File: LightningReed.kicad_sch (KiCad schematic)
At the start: 163 parts, among them P1 Conn_WallPlug, Q1 NCE65T180D, Q10 DMZ6005E, Q11 2N7002K, Q12 NCEP15T14D, Q13 BSS123, Q2 2N7002, Q3 Q_NMOS_GDS, Q4 2N7002, Q5 2N7002K, Q6 2N7002K, Q7 NCE65T260K, Q8 NCE65T260K, Q9 NCE0102, T1 Transformer_2P_2S, U1 UCC28056, U2 78L05S, U3 LMC7111, U4 UCC28780, U5 UCC27712, U6 LM317G, U7 FODM8801A, U8 TL431DBZ, U9 UCC24612-1DBV

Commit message: C Footprint
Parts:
- C11, C12, C13, C14, C15, C23, C24, C25, C26, C30, C31, C32, C33, C34, C35, C36, C37, C38, C44, C45, C46, C47: footprint (none) -> Capacitor_SMD:C_0603_1608Metric
- C16, C28: footprint (none) -> Capacitor_SMD:C_0805_2012Metric
- C17: value 33nF -> 220pF; footprint (none) -> Capacitor_SMD:C_0603_1608Metric
- C18, C39, C40, C41, C42: footprint (none) -> Capacitor_SMD:C_1206_3216Metric
- C19: footprint (none) -> Capacitor_SMD:C_1812_4532Metric
- C20, C21, C22, C27, C29: footprint (none) -> Capacitor_SMD:C_1210_3225Metric
- C43: footprint (none) -> Capacitor_SMD:CP_Elec_10x10
- D1: footprint (none) -> Diode_SMD:D_SMF
- D2: footprint (none) -> LightningReed:UMSB
- D3, D5: footprint (none) -> Diode_SMD:D_SOD-123F
- D4: footprint (none) -> Diode_SMD:D_SOD-323
- D6: footprint (none) -> Diode_SMD:D_SOD-123
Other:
- note added: "VZT681M1ETR-1010"
- moved on the sheet: R49

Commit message: Footprints
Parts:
- D10, D15: footprint (none) -> Diode_SMD:D_SOD-123
- D11, D13, D14, D16: footprint (none) -> Diode_SMD:D_SOD-323
- D12: footprint (none) -> Package_TO_SOT_SMD:SOT-23
- D17: footprint (none) -> Diode_SMD:D_SOD-523
- D7: value ES1JAF -> STTH1R06A; footprint (none) -> Diode_SMD:D_SMA
- D8, D9: footprint (none) -> Diode_SMD:D_SOD-123F
- L1, L2: footprint (none) -> LightningReed:CHOKE
- L3: value PDMTAT068125-151MLU -> SDA0912-150uH-0.45; footprint (none) -> Inductor_THT:L_Radial_D12.0mm_P5.00mm_Fastron_11P
- L4: footprint (none) -> Inductor_SMD:L_12x12mm_H8mm
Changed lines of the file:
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@@
       (effects (font (size 0.8 0.8)))
     )
-    (property "Footprint" "" (at 266.065 78.74 90)
+    (property "Footprint" "Diode_SMD:D_SOD-123" (at 266.065 78.74 90)
       (effects (font (size 1.27 1.27)) hide)
     )
@@
       (effects (font (size 1.27 1.27)))
     )
-    (property "Footprint" "" (at 57.785 31.75 0)
+    (property "Footprint" "LightningReed:CHOKE" (at 57.785 31.75 0)
       (effects (font (size 1.27 1.27)) hide)
     )
@@
       (effects (font (size 0.8 0.8)) (justify left))
     )
-    (property "Footprint" "" (at 252.73 130.81 90)
+    (property "Footprint" "Diode_SMD:D_SOD-323" (at 252.73 130.81 90)
       (effects (font (size 1.27 1.27)) hide)
     )
@@
       (effects (font (size 1.27 1.27)) (justify right))
     )
-    (property "Footprint" "" (at 293.37 79.375 90)
+    (property "Footprint" "Diode_SMD:D_SOD-523" (at 293.37 79.375 90)
       (effects (font (size 1.27 1.27)) hide)
     )
@@
       (effects (font (size 0.8 0.8)) (justify left))
     )
-    (property "Footprint" "" (at 271.145 97.79 90)
+    (property "Footprint" "Diode_SMD:D_SOD-323" (at 271.145 97.79 90)
       (effects (font (size 1.27 1.27)) hide)
     )
@@
       (effects (font (size 0.8 0.8)))
     )
-    (property "Footprint" "" (at 226.06 95.25 90)
+    (property "Footprint" "Package_TO_SOT_SMD:SOT-23" (at 226.06 95.25 90)
       (effects (font (size 1.27 1.27)) hide)
     )
@@
       (effects (font (size 0.8 0.8)) (justify left))
     )
-    (property "Footprint" "" (at 241.3 130.81 90)
+    (property "Footprint" "Diode_SMD:D_SOD-323" (at 241.3 130.81 90)
       (effects (font (size 1.27 1.27)) hide)
     )
@@
       (effects (font (size 1.27 1.27)))
     )
-    (property "Footprint" "" (at 84.455 31.75 0)
+    (property "Footprint" "LightningReed:CHOKE" (at 84.455 31.75 0)
       (effects (font (size 1.27 1.27)) hide)
     )
@@
       (effects (font (size 1.27 1.27)))
     )
-    (property "Value" "PDMTAT068125-151MLU" (at 38.735 53.34 90)
+    (property "Value" "SDA0912-150uH-0.45" (at 38.735 53.34 90)
       (effects (font (size 1.27 1.27)))
     )
-    (property "Footprint" "" (at 38.735 56.515 0)
+    (property "Footprint" "Inductor_THT:L_Radial_D12.0mm_P5.00mm_Fastron_11P" (at 38.735 56.515 0)
       (effects (font (size 1.27 1.27)) hide)
     )
@@
       (effects (font (size 1.27 1.27)))
     )
-    (property "Value" "ES1JAF" (at 187.325 40.64 0)
+    (property "Value" "STTH1R06A" (at 189.865 41.91 0)
       (effects (font (size 1.27 1.27)))
     )
-    (property "Footprint" "" (at 191.77 39.37 90)
+    (property "Footprint" "Diode_SMD:D_SMA" (at 191.77 39.37 90)
       (effects (font (size 1.27 1.27)) hide)
     )
@@
       (effects (font (size 0.8 0.8)) (justify right))
     )
-    (property "Footprint" "" (at 235.585 69.215 90)
+    (property "Footprint" "Diode_SMD:D_SOD-123F" (at 235.585 69.215 90)
       (effects (font (size 1.27 1.27)) hide)
     )
@@
       (effects (font (size 0.8 0.8)) (justify right))
     )
-    (property "Footprint" "" (at 207.01 90.805 90)
+    (property "Footprint" "Diode_SMD:D_SOD-323" (at 207.01 90.805 90)
       (effects (font (size 1.27 1.27)) hide)
     )
@@
       (effects (font (size 1.27 1.27)))
     )
-    (property "Footprint" "" (at 63.5 62.865 0)
+    (property "Footprint" "Inductor_SMD:L_12x12mm_H8mm" (at 63.5 62.865 0)
       (effects (font (size 1.27 1.27)) hide)
     )
@@
       (effects (font (size 0.8 0.8)) (justify right))
     )
-    (property "Footprint" "" (at 240.665 69.215 90)
+    (property "Footprint" "Diode_SMD:D_SOD-123F" (at 240.665 69.215 90)
       (effects (font (size 1.27 1.27)) hide)
     )
@@
       (effects (font (size 0.8 0.8)) (justify right))
     )
-    (property "Footprint" "" (at 220.345 81.28 90)
+    (property "Footprint" "Diode_SMD:D_SOD-123" (at 220.345 81.28 90)
       (effects (font (size 1.27 1.27)) hide)
     )

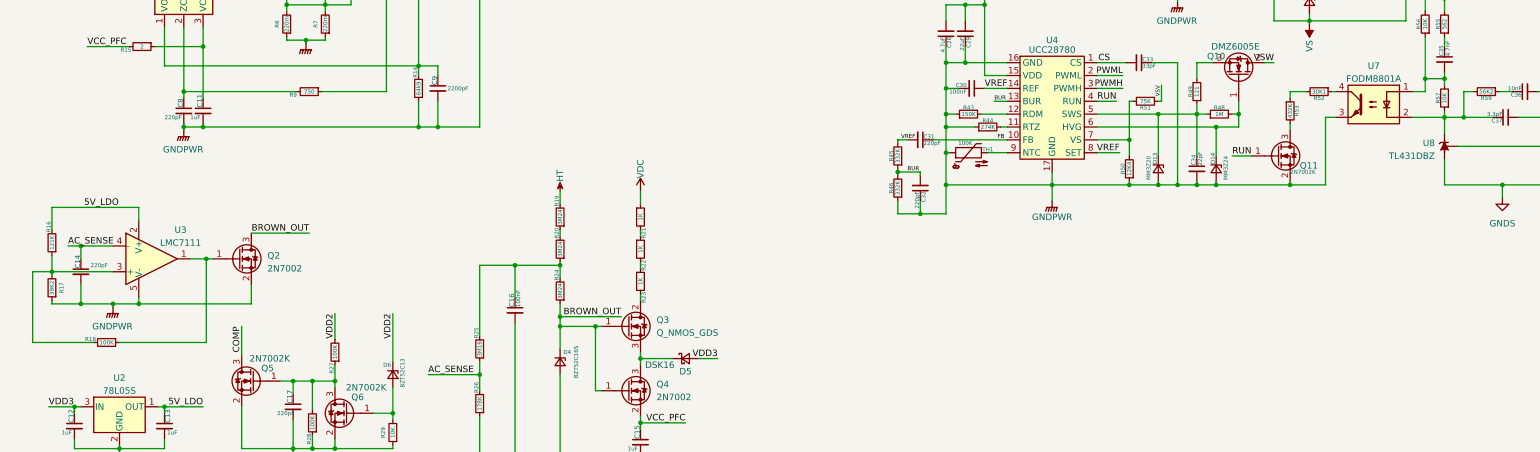
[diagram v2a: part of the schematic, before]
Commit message: Complete footprints
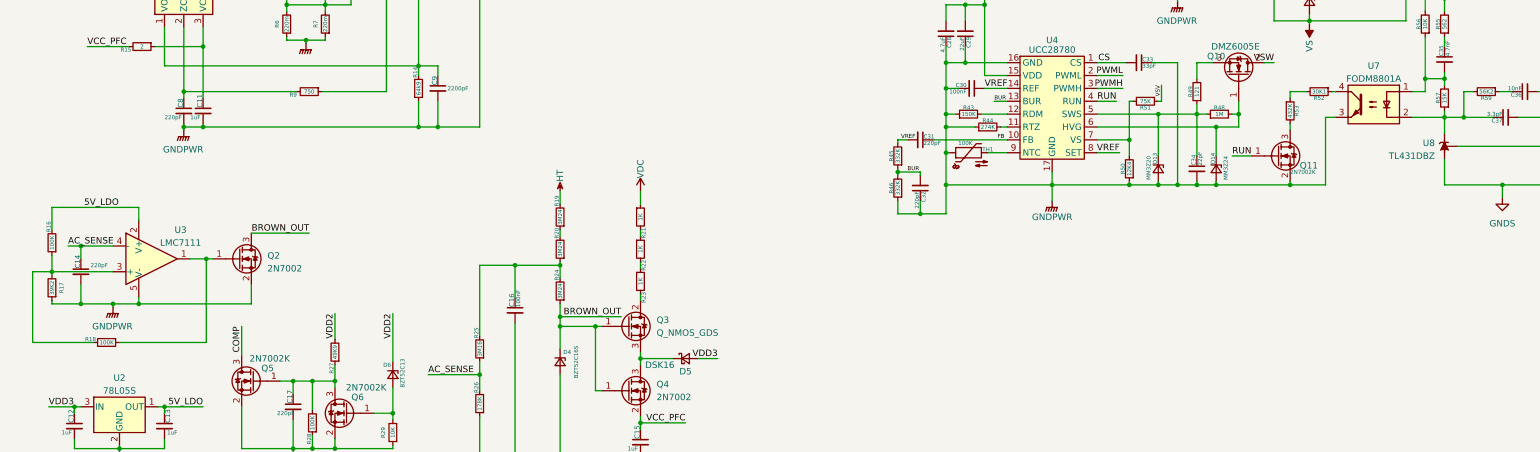
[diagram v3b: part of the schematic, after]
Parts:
- L5: footprint (none) -> LightningReed:CKST0603
- L6: footprint (none) -> Inductor_SMD:L_0805_2012Metric
- P1: footprint (none) -> Connector_Wire:SolderWire-1sqmm_1x02_P5.4mm_D1.4mm_OD2.7mm
- Q1: footprint (none) -> Package_TO_SOT_SMD:TO-263-2
- Q10, Q9: footprint (none) -> Package_TO_SOT_SMD:SOT-23
- Q7, Q8: footprint (none) -> Package_TO_SOT_SMD:TO-252-2
- R1, R13, R14, R15, R17, R18, R26, R28, R29, R31, R32, R33, R34, R35, R36, R37, R42, R43, R44, R45, R46, R47, R48, R49, R5, R50, R51, R52, R53, R54, R55, R56, R58, R59, R60, R62, R63, R8, R9, TH1: footprint (none) -> Resistor_SMD:R_0603_1608Metric
- R10, R11, R12, R19, R2, R20, R21, R22, R23, R24, R3, R30, R38, R39, R4, R6, R7: footprint (none) -> Resistor_SMD:R_1206_3216Metric
- R16: value 121K -> 100K; footprint (none) -> Resistor_SMD:R_0603_1608Metric
- R25, R40, R41, R61: footprint (none) -> Resistor_SMD:R_0805_2012Metric
- R27: value 100K -> 49K9; footprint (none) -> Resistor_SMD:R_0603_1608Metric
- R57: value 10K -> 15K; footprint (none) -> Resistor_SMD:R_0603_1608Metric
- U1: footprint (none) -> Package_TO_SOT_SMD:SOT-23-6
- U3: footprint (none) -> Package_TO_SOT_SMD:SOT-23-5
- U4: footprint (none) -> Package_DFN_QFN:QFN-16-1EP_3x3mm_P0.5mm_EP1.45x1.45mm
- U5: footprint (none) -> Package_SO:SO-8_3.9x4.9mm_P1.27mm

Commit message: Finish footprints
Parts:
- C3: footprint (none) -> Capacitor_SMD:C_1812_4532Metric
- Q3: value Q_NMOS_GDS -> 1N60G; footprint (none) -> Package_TO_SOT_SMD:SOT-223
- T1: footprint (none) -> LightningReed:RM10
- TP1, TP2, TP3, TP4: footprint (none) -> Connector_Wire:SolderWire-0.5sqmm_1x01_D0.9mm_OD2.1mm
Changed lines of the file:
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@@
       (effects (font (size 1.27 1.27)) (justify left))
     )
-    (property "Value" "Q_NMOS_GDS" (at 142.24 163.195 0)
-      (effects (font (size 1.27 1.27)) (justify left))
-    )
-    (property "Footprint" "" (at 141.605 159.385 0)
+    (property "Value" "1N60G" (at 142.24 163.195 0)
+      (effects (font (size 1.27 1.27)) (justify left))
+    )
+    (property "Footprint" "Package_TO_SOT_SMD:SOT-223" (at 141.605 159.385 0)
       (effects (font (size 1.27 1.27)) hide)
     )
@@
       (effects (font (size 1.27 1.27)) (justify left))
     )
-    (property "Footprint" "" (at 360.68 104.14 0)
+    (property "Footprint" "Connector_Wire:SolderWire-0.5sqmm_1x01_D0.9mm_OD2.1mm" (at 360.68 104.14 0)
       (effects (font (size 1.27 1.27)) hide)
     )
@@
       (effects (font (size 1.27 1.27)))
     )
-    (property "Footprint" "" (at 257.81 33.655 0)
+    (property "Footprint" "LightningReed:RM10" (at 257.81 33.655 0)
       (effects (font (size 1.27 1.27)) hide)
     )
@@
       (effects (font (size 1.27 1.27)) (justify left))
     )
-    (property "Footprint" "" (at 360.68 70.485 0)
+    (property "Footprint" "Connector_Wire:SolderWire-0.5sqmm_1x01_D0.9mm_OD2.1mm" (at 360.68 70.485 0)
       (effects (font (size 1.27 1.27)) hide)
     )
@@
       (effects (font (size 1.27 1.27)) (justify left))
     )
-    (property "Footprint" "" (at 360.68 94.615 0)
+    (property "Footprint" "Connector_Wire:SolderWire-0.5sqmm_1x01_D0.9mm_OD2.1mm" (at 360.68 94.615 0)
       (effects (font (size 1.27 1.27)) hide)
     )
@@
       (effects (font (size 1.27 1.27)) (justify left))
     )
-    (property "Footprint" "" (at 45.085 62.865 0)
+    (property "Footprint" "Capacitor_SMD:C_1812_4532Metric" (at 45.085 62.865 0)
       (effects (font (size 1.27 1.27)) hide)
     )
@@
       (effects (font (size 1.27 1.27)) (justify left))
     )
-    (property "Footprint" "" (at 360.68 81.915 0)
-      (effects (font (size 1.27 1.27)) hide)
-    )
+    (property "Footprint" "Connector_Wire:SolderWire-0.5sqmm_1x01_D0.9mm_OD2.1mm" (at 360.68 81.915 0)
+      (effects (font (size 1.27 1.27)) hide)
+    )

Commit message: routing 1/?
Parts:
- Q12: footprint Package_TO_SOT_SMD:LFPAK33 -> Package_TO_SOT_SMD:TO-263-2
- Q3: footprint Package_TO_SOT_SMD:SOT-223 -> Package_TO_SOT_SMD:SOT-223-3_TabPin2
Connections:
- net GNDPWR: now also D12.1 (A); no longer D12.2 (A)
- net VDC: now also T1.4 (AB); no longer T1.2 (AB)
- net at C1.1, L1.2: now also L2.1; no longer L2.2
- net at C1.2, L1.4: now also L2.3; no longer L2.4
- net at Q9.1 (G), R42.1: now also D12.3 (K); no longer D12.1 (K)
- net at D9.2 (A): now also T1.5 (SC); no longer T1.4 (SC)
- net at D2.4: now also L2.2; no longer L2.1
- net at D2.3: now also L2.4; no longer L2.3
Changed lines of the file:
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@@
       (effects (font (size 1.27 1.27)) (justify left))
     )
-    (property "Footprint" "Package_TO_SOT_SMD:SOT-223" (at 141.605 159.385 0)
+    (property "Footprint" "Package_TO_SOT_SMD:SOT-223-3_TabPin2" (at 141.605 159.385 0)
       (effects (font (size 1.27 1.27)) hide)
     )
@@
     )
   )
-  (symbol (lib_id "Device:D_Zener_Small") (at 226.06 95.25 0) (unit 1)
+  (symbol (lib_name "D_Zener_Small_1") (lib_id "Device:D_Zener_Small") (at 226.06 95.25 0) (unit 1)
     (in_bom yes) (on_board yes) (dnp no)
     (property "Reference" "D12" (at 223.52 94.615 0)
@@
     )
     (pin "1")
-    (pin "2")
+    (pin "3")
     (instances
       (project "LightningReed"
@@
     (pin "10")
     (pin "13")
-    (pin "2")
     (pin "4")
+    (pin "5")
     (pin "6")
     (pin "7")
@@
     )
   )
-  (symbol (lib_id "Device:L_Coupled_Small") (at 84.455 31.75 0) (mirror y) (unit 1)
-    (in_bom yes) (on_board yes) (dnp no) (fields_autoplaced)
+  (symbol (lib_id "Device:L_Coupled_Small") (at 84.455 31.75 0) (unit 1)
+    (in_bom yes) (on_board yes) (dnp no)
     (property "Reference" "L2" (at 84.455 25.4 0)
       (effects (font (size 1.27 1.27)))
@@
       (effects (font (size 0.8 0.8)))
     )
-    (property "Footprint" "Package_TO_SOT_SMD:LFPAK33" (at 294.64 20.955 0)
-      (effects (font (size 1.27 1.27)) hide)
-    )
+    (property "Footprint" "Package_TO_SOT_SMD:TO-263-2" (at 294.64 20.955 0)
+      (effects (font (size 1.27 1.27)) hide)
+    )

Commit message: SR layout
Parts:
- added TP10, TP11, TP12, TP13, TP14, TP15, TP16, TP9: TestPoint, Connector_Wire:SolderWire-0.15sqmm_1x01_D0.5mm_OD1.5mm, symbol Connector:TestPoint
- added TP5, TP6, TP7, TP8: TestPoint, Connector_Wire:SolderWire-1sqmm_1x01_D1.4mm_OD2.7mm, symbol Connector:TestPoint
- TP1: footprint Connector_Wire:SolderWire-0.5sqmm_1x01_D0.9mm_OD2.1mm -> Connector_Wire:SolderWire-1sqmm_1x01_D1.4mm_OD2.7mm
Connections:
- net GNDPWR: now also TP14.1; no longer U7.3
- net GNDS: now also TP7.1; no longer T1.13 (SB)
- net VAUX: now also TP12.1; no longer T1.8 (SC)
- net VS: now also TP11.1; no longer T1.10 (SD)
- net at R52.1: now also TP13.1; no longer U7.4
- net at C38.1, Q12.3 (S), U9.2 (VS): now also TP5.1; no longer T1.9 (SA)
- new net: TP16.1, U7.3
- new net: T1.9 (SA), TP6.1
- new net: T1.10 (SD), TP10.1
- new net: T1.13 (SB), TP8.1
- new net: T1.8 (SC), TP9.1
- new net: TP15.1, U7.4
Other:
- moved on the sheet: C35, C36, C37, R54, R55, R56, R57, R58, R59, R60, TP1, TP2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
